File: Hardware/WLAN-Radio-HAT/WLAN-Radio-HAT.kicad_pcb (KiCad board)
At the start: 2 copper layers, 65 x 30 mm, 35 parts, among them J1 Pi, J2 Amp, J3 LCD, J4 Next, J5 Prev, J6 Supply, U1 PCM5100A, U2 AMP150

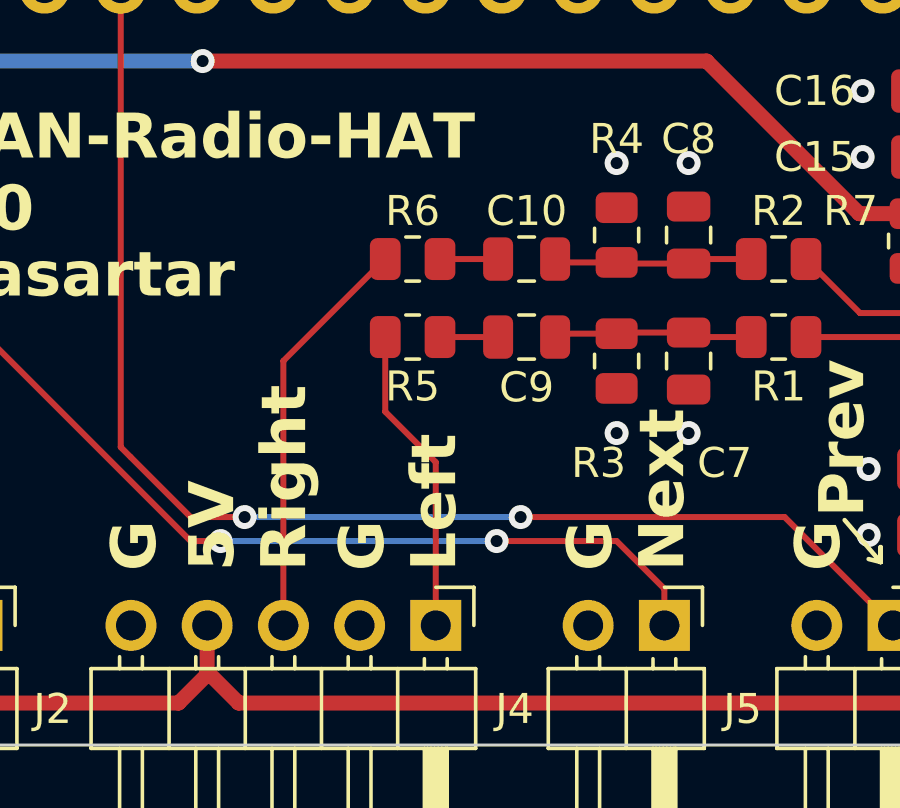
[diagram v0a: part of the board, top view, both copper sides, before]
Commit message: removed unnecessary filter components
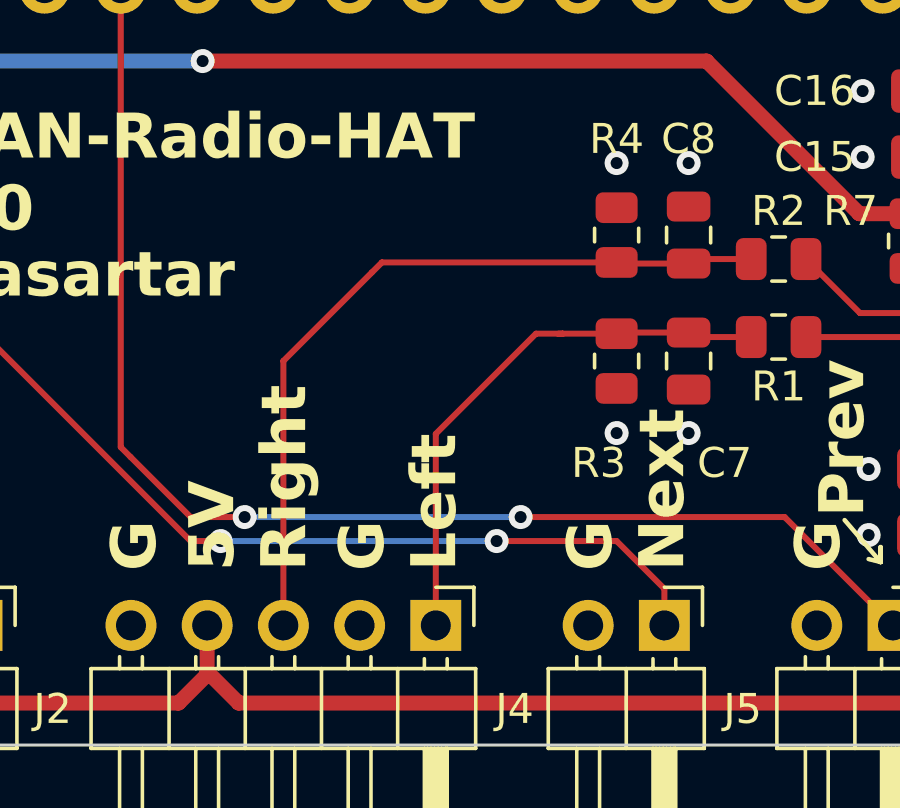
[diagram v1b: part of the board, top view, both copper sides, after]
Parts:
- removed C10, C9: 0R, Capacitor_SMD:C_0805_2012Metric
- removed R5, R6: 0R, Resistor_SMD:R_0805_2012Metric
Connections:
- C7 pad 1: Net-(C7-Pad1) -> Net-(J2-Pin_1)
- C8 pad 1: Net-(C10-Pad1) -> Net-(J2-Pin_3)
- R1 pad 2: Net-(C7-Pad1) -> Net-(J2-Pin_1)
- R2 pad 2: Net-(C10-Pad1) -> Net-(J2-Pin_3)
- R3 pad 1: Net-(C7-Pad1) -> Net-(J2-Pin_1)
- R4 pad 1: Net-(C10-Pad1) -> Net-(J2-Pin_3)
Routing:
- net Net-(J2-Pin_3): track 13.6 -> 25.8 mm
- net Net-(J2-Pin_1): track 10.3 -> 18.5 mm
- net Net-(C7-Pad1): track 6.66 -> 0.00 mm
- net Net-(C10-Pad1): track 6.66 -> 0.00 mm
- net Net-(C9-Pad2): track 1.94 -> 0.00 mm
- net Net-(C10-Pad2): track 1.94 -> 0.00 mm

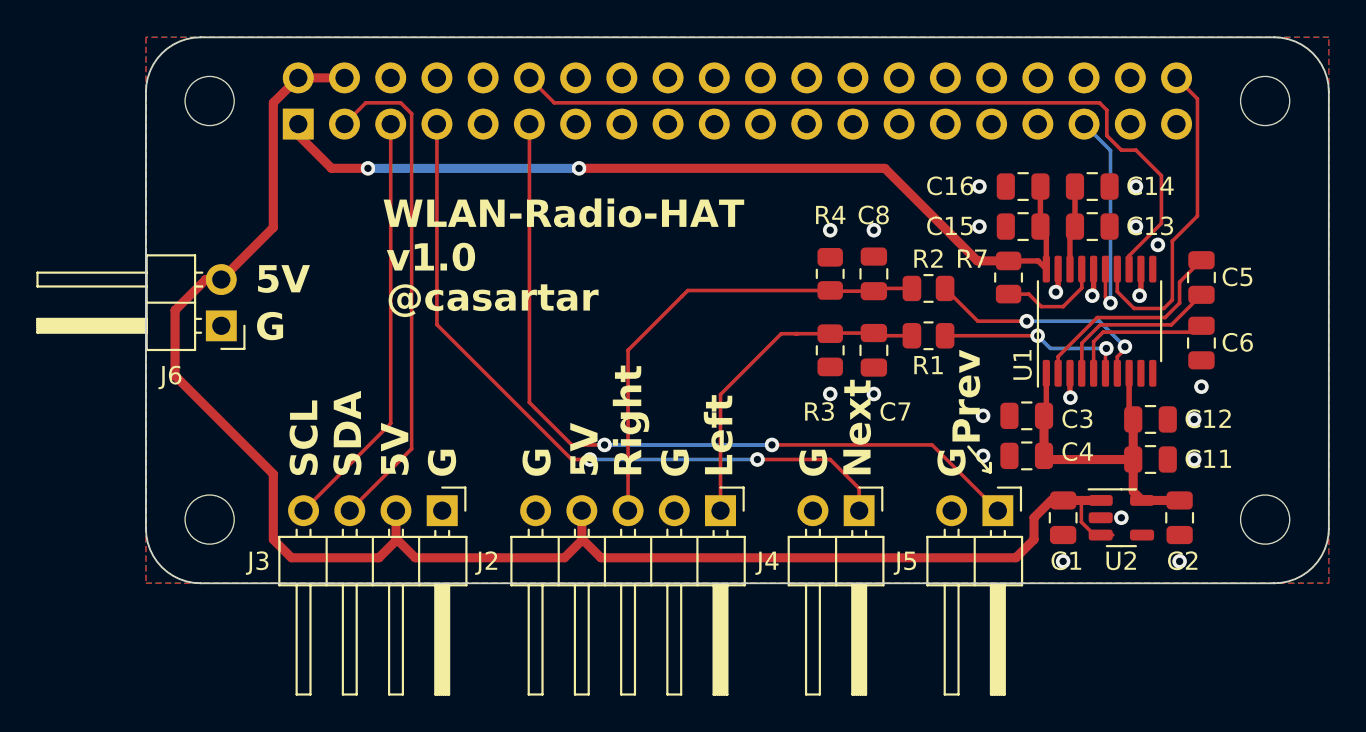
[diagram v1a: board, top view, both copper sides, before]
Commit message: add alternate LCD connector and use better 3v3 supply pin
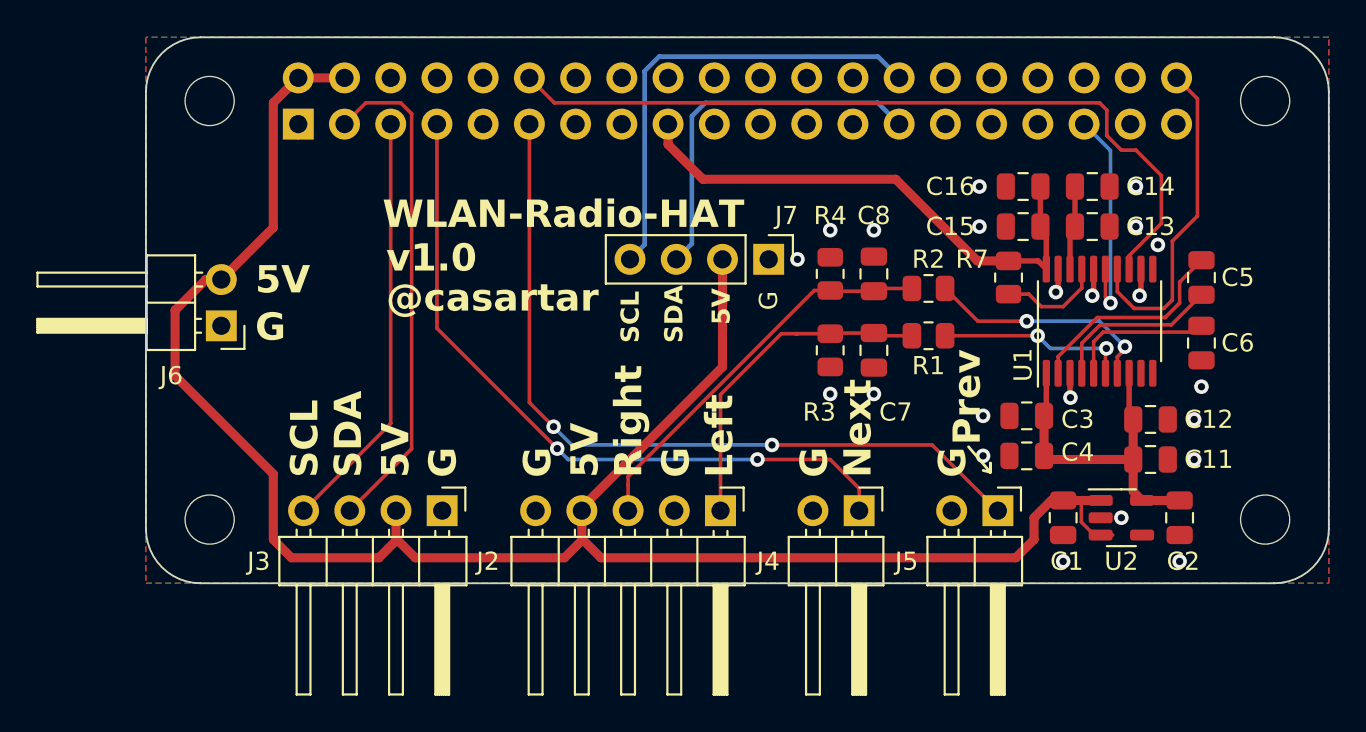
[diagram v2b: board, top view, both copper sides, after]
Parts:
- added J7: LCD, Connector_PinHeader_2.54mm:PinHeader_1x04_P2.54mm_Vertical, F.Cu at (134.2, 82.2)
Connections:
- J1 pad 1: +3V3 -> unconnected-(J1-Pin_1-Pad1)
- J1 pad 17: unconnected-(J1-Pin_17-Pad17) -> +3V3
- J1 pad 27: unconnected-(J1-Pin_27-Pad27) -> LCD_SDA_ALT
- J1 pad 28: unconnected-(J1-Pin_28-Pad28) -> LCD_SCL_ALT
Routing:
- net LCD_SCL_ALT: track 0.00 -> 25.5 mm
- net LCD_SDA_ALT: track 0.00 -> 20.4 mm
- net +3V3: track 49.4 -> 29.4 mm, vias 2 -> 0
- net +5V: track 89.5 -> 106.5 mm
- net Net-(J2-Pin_3): track 25.8 -> 21.8 mm
- net unconnected-(J1-Pin_1-Pad1): track 0.00 -> 0.60 mm
- net GND: vias 21 -> 22
